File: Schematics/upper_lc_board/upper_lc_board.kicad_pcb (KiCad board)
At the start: 4 copper layers, 69.5 x 60 mm, 123 parts, among them J1 Stack Male Edge Connector, J2 HAL_SENS, J3 PT1, J4 PT2, J5 SOL_CONN, J6 SOL2_CONN, J7 TC, J8 USB_C_Female_USB2_Small, Q1 MOSFET_BSS138, U1 ESP32-S3-WROOM-1-N16R2, U10 OA-TLV9001IDCK, U11 OA-TLV9001IDCK, U12 OA-TLV9001IDCK, U2 CAN_TRX_SN65HVD230DR, U3 PD_D3V3XA4B10LP, U4 PMUX_TPS2121RUXR, U5 TMP117MAIDRVR, U6 TLV75801PDRV, U7 ADC_ADS131M04IPWR, U8 SSR_VO1400AEFTR, U9 OA-TLV9001IDCK

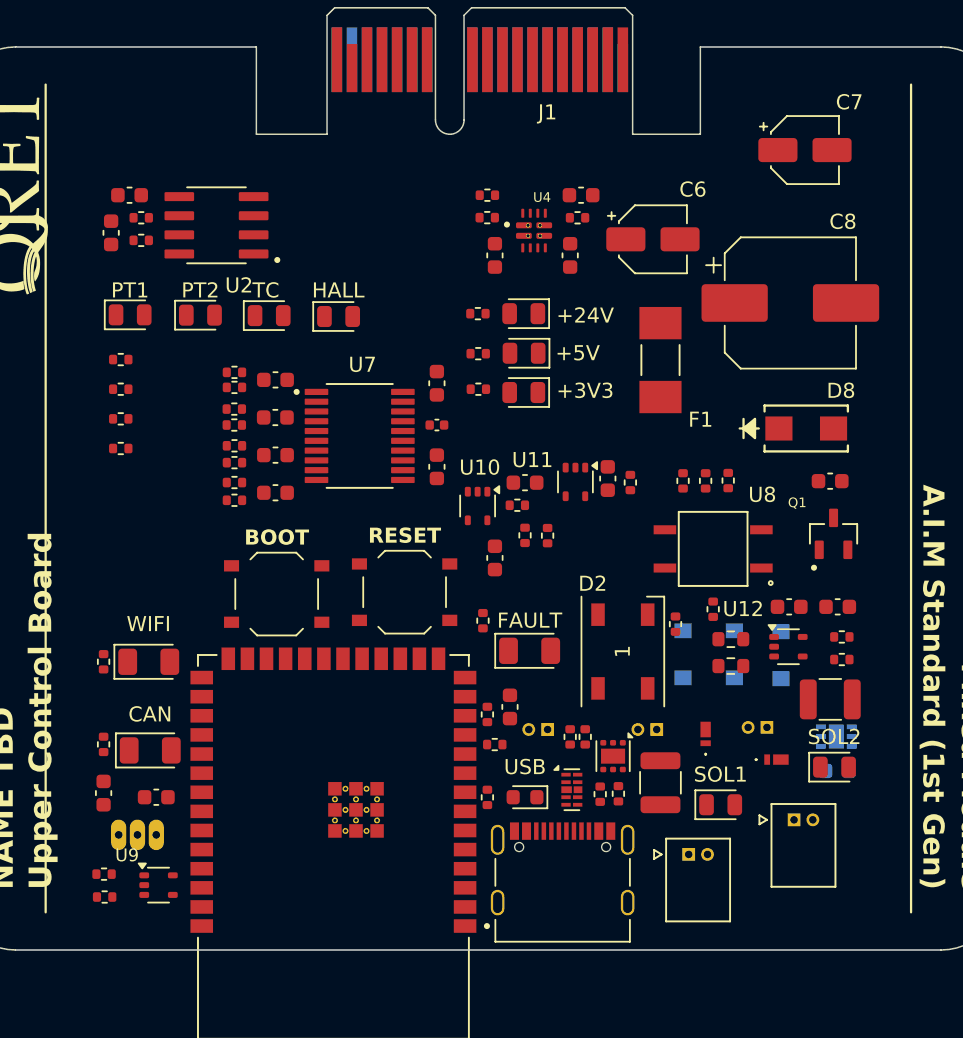
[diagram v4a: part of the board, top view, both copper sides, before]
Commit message: add vertical connectors, revert MUX circuitry to ORing setup w ideal diodes
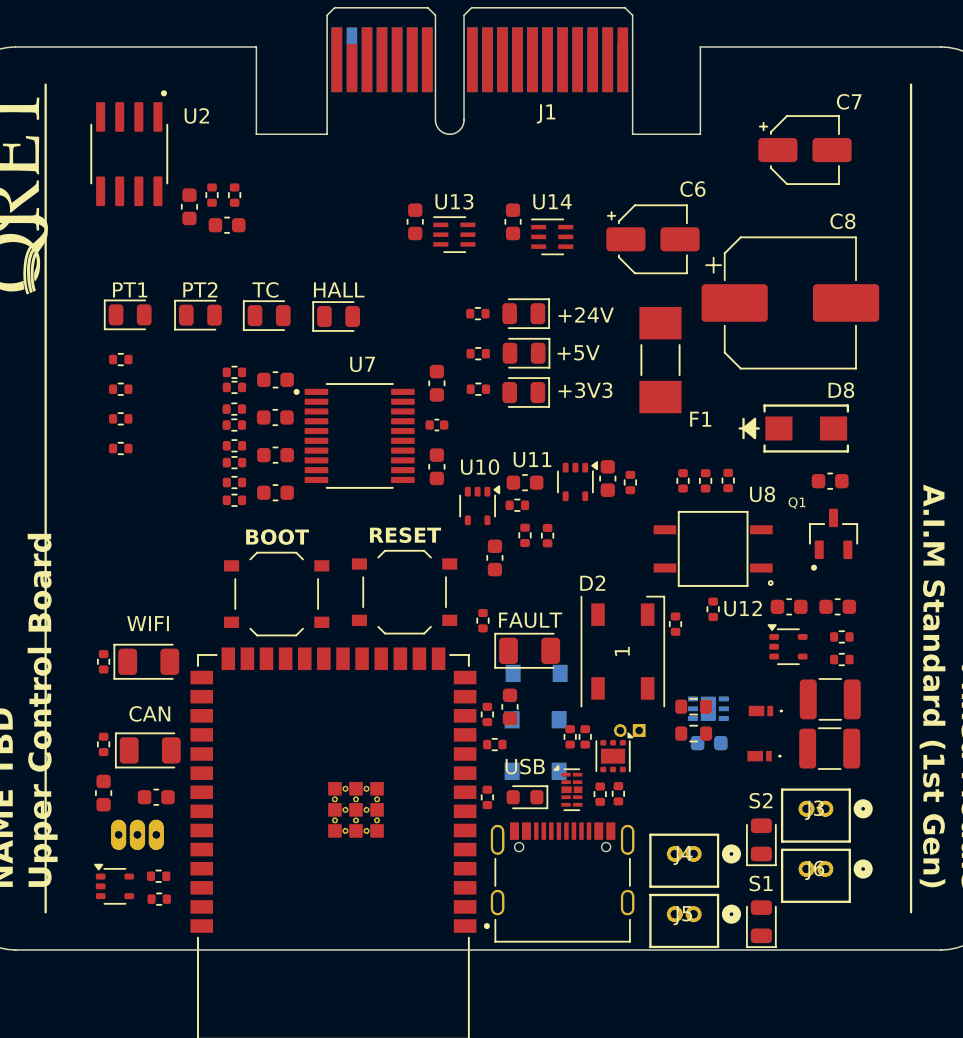
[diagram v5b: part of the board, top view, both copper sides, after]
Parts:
- removed C10, C9: 1uF, Capacitor_SMD:C_0603_1608Metric
- removed C13: 10uF, Capacitor_SMD:C_0603_1608Metric
- removed R11: 68k, Resistor_SMD:R_0402_1005Metric
- removed R12: 18k, Resistor_SMD:R_0402_1005Metric
- removed R25: 10k, Resistor_SMD:R_0402_1005Metric
- removed U4: PMUX_TPS2121RUXR, TPS2121RUXR:IC_TPS2121RUXR
- added C32: 1uF, Capacitor_SMD:C_0603_1608Metric, F.Cu at (126.0, 78.0)
- added C33: 1uF, Capacitor_SMD:C_0603_1608Metric, F.Cu at (132.5, 78.0)
- added U13: ID_LM66100DCKR, LM66100:SC-70-6, F.Cu at (128.6, 78.8)
- added U14: ID_LM66100DCKR, LM66100:SC-70-6, F.Cu at (135.1, 79.0)
- J3, J4: footprint 530480210:MOLEX_530480210 -> CONNS:CONN02_530470260_MOL; moved to F.Cu
- J5, J6: footprint 530480210:MOLEX_530480210 -> CONNS:CONN02_530470260_MOL
- moved CR3 16.3 mm to (134.1, 108.0), turned to 0 degrees
- moved CR2 13.9 mm to (134.0, 111.1), turned to 0 degrees
- moved J4 12.8 mm to (144.5, 120.0), turned to 0 degrees
- moved CR1 12.5 mm to (134.0, 114.5), turned to 0 degrees
- moved J3 12.4 mm to (153.2, 117.0), turned to 0 degrees
- moved R20 11.5 mm to (153.5, 113.0), turned to 180 degrees
- moved U5 8.70 mm to (145.5, 110.3)
- moved C29 8.70 mm to (145.5, 112.6)
- moved J7 8.49 mm to (140.9, 111.8)
- moved S1 8.23 mm to (149.0, 124.5), turned to 90 degrees
- moved C28 7.72 mm to (113.5, 78.2), turned to 180 degrees
- moved U2 7.48 mm to (107.0, 73.5), turned to -90 degrees
- moved R41 6.89 mm to (114.0, 76.2), turned to 90 degrees
- moved S2 6.85 mm to (149.0, 119.1), turned to 90 degrees
- moved R46 5.12 mm to (144.5, 110.2)
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- renumbered SOL1 to S1, SOL2 to S2

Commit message: finish adding components to layout, revise layout next.
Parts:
- removed C12, C4: 0.1uF, Capacitor_SMD:C_0603_1608Metric
- C3, C5: moved to B.Cu
- C6: value 10uF_12V -> 22uF_12V
- C7: value 10uF_16V -> 22uF_16V
- C8: value 47uF_63V -> 100uF_50V
- moved C5 85.4 mm to (127.5, 124.5), turned to 90 degrees
- moved C2 82.3 mm to (111.5, 104.2), turned to 90 degrees
- moved C3 77.2 mm to (126.0, 124.5), turned to -90 degrees
- moved C1 68.6 mm to (132.5, 113.7), turned to 90 degrees
- moved R3 61.9 mm to (131.0, 113.5), turned to -90 degrees
- moved R6 28.1 mm to (111.5, 101.0), turned to 0 degrees
- moved R7 26.8 mm to (111.5, 102.0), turned to 180 degrees
- moved R27 8.76 mm to (146.0, 112.5), turned to -90 degrees
- moved C11 8.13 mm to (139.5, 114.0), turned to 0 degrees
- moved R15 6.58 mm to (137.0, 116.0), turned to -90 degrees
- moved R19 5.03 mm to (139.4, 100.3), turned to 180 degrees
- moved R46 4.55 mm to (145.2, 114.7)
- moved R47 4.55 mm to (145.2, 116.5)
- moved R48 4.40 mm to (142.5, 117.2), turned to 180 degrees
- moved C26 3.81 mm to (139.7, 98.8), turned to 0 degrees
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
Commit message: temp commit for CJC alternative change
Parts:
- C29, C5, CR1, CR2, CR3, U5: moved to F.Cu
- moved D2 33.1 mm to (107.5, 99.2)
- moved R2 33.1 mm to (111.2, 96.5)
- moved CR1 8.65 mm to (138.5, 107.1), turned to 180 degrees
- moved CR3 4.53 mm to (137.6, 110.9), turned to -90 degrees
- moved C28 3.98 mm to (116.9, 76.2)
- moved C3 3.39 mm to (125.4, 121.2), turned to 0 degrees
- moved C29 2.88 mm to (145.9, 109.8), turned to 90 degrees
- moved U5 2.48 mm to (143.1, 111.1), turned to 0 degrees
- moved D15 2.31 mm to (111.6, 81.9)
- moved D14 2.31 mm to (107.0, 81.9)
- moved D16 2.31 mm to (116.2, 81.9)
- moved D17 2.31 mm to (120.8, 82.0)
- moved R28 2.31 mm to (106.3, 84.8)
- moved R29 2.31 mm to (106.3, 86.8)
- moved R30 2.31 mm to (106.3, 88.8)
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
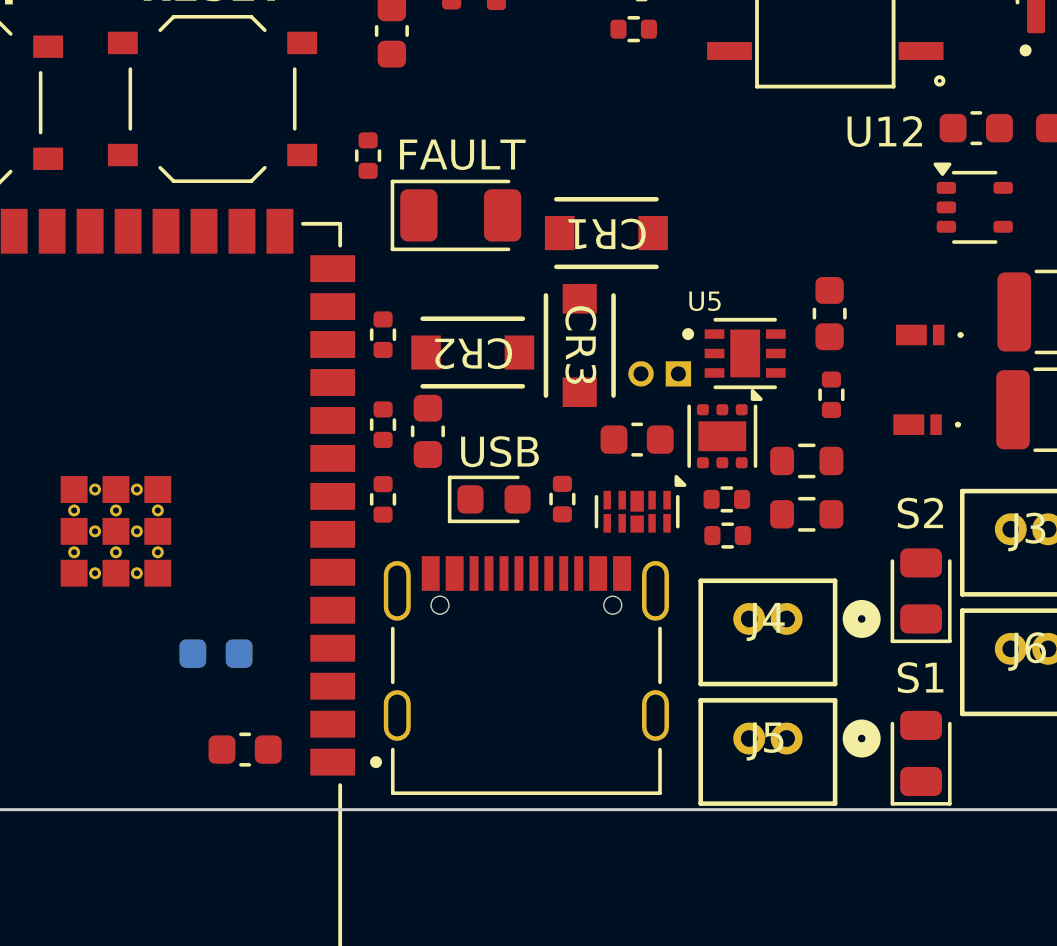
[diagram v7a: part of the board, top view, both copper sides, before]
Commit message: add thermistor circuitry & update layout
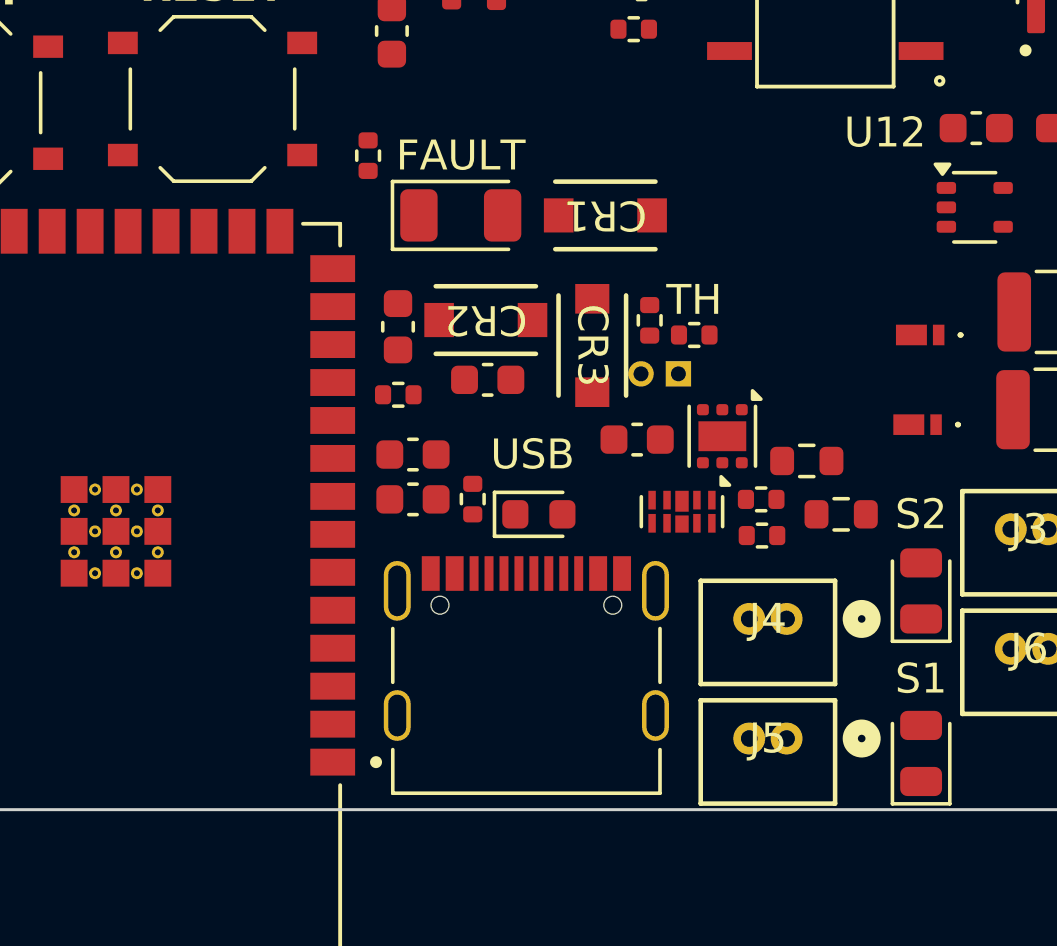
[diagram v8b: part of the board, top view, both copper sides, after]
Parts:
- removed C29: 0.1uF, Capacitor_SMD:C_0603_1608Metric
- removed R27, R42, R43: 4.7k, Resistor_SMD:R_0402_1005Metric
- removed U5: TMP117MAIDRVR, TMP117MAIDRVR:SON65P200X200X80-7N
- added C4: 0.1uF, Capacitor_SMD:C_0603_1608Metric, F.Cu at (131.5, 110.2)
- added R5: 10k, Resistor_SMD:R_0402_1005Metric, F.Cu at (139.9, 110.0)
- added TH: Thermistor, Resistor_SMD:R_0402_1005Metric, F.Cu at (141.4, 110.5)
- C3: moved to F.Cu
- moved C5 10.1 mm to (132.0, 116.0), turned to 180 degrees
- moved C3 9.37 mm to (132.0, 114.5), turned to 180 degrees
- moved R15 3.00 mm to (134.0, 116.0), turned to 90 degrees
- moved C1 2.64 mm to (134.5, 112.0), turned to 180 degrees
- moved USB 1.58 mm to (136.2, 116.5)
- moved U3 1.50 mm to (141.0, 116.4)
- moved CR2 1.17 mm to (134.4, 110.0)
- moved R48 1.15 mm to (143.7, 117.2)
- moved R49 1.15 mm to (143.7, 116.0)
- moved R47 1.15 mm to (146.3, 116.5)
- moved R3 1.12 mm to (131.5, 112.5), turned to 0 degrees
- moved CR1 0.59 mm to (138.4, 106.5)
- moved CR3 0.42 mm to (138.0, 110.9)
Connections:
- U1 pad 7: GPIO_7 -> /ESP Breakout Cirucitry/GPIO_7
